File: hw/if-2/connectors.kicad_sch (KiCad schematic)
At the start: 3 parts, among them J1 DB25_Socket, J2 PJ-102AH, J3 Conn_02x12_Odd_Even

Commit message: Documentation improvements, moved a OVP circuit
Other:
- note added: "See: AMP L77SDB25SA4CH4F"
- title: COS/CTCSS/PTT Controls (Radio 1) -> Connectors
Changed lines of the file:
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@@
 	(paper "USLetter")
 	(title_block
-		(title "COS/CTCSS/PTT Controls (Radio 1)")
-		(date "2025-05-13")
+		(title "Connectors")
+		(date "2025-05-31")
 		(rev "2")
 		(company "Bruce MacKinnon KC1FSZ")
@@
 			)
 		)
+	)
+	(text "See: AMP L77SDB25SA4CH4F"
+		(exclude_from_sim no)
+		(at 101.6 118.618 0)
+		(effects
+			(font
+				(size 1.27 1.27)
+			)
+		)

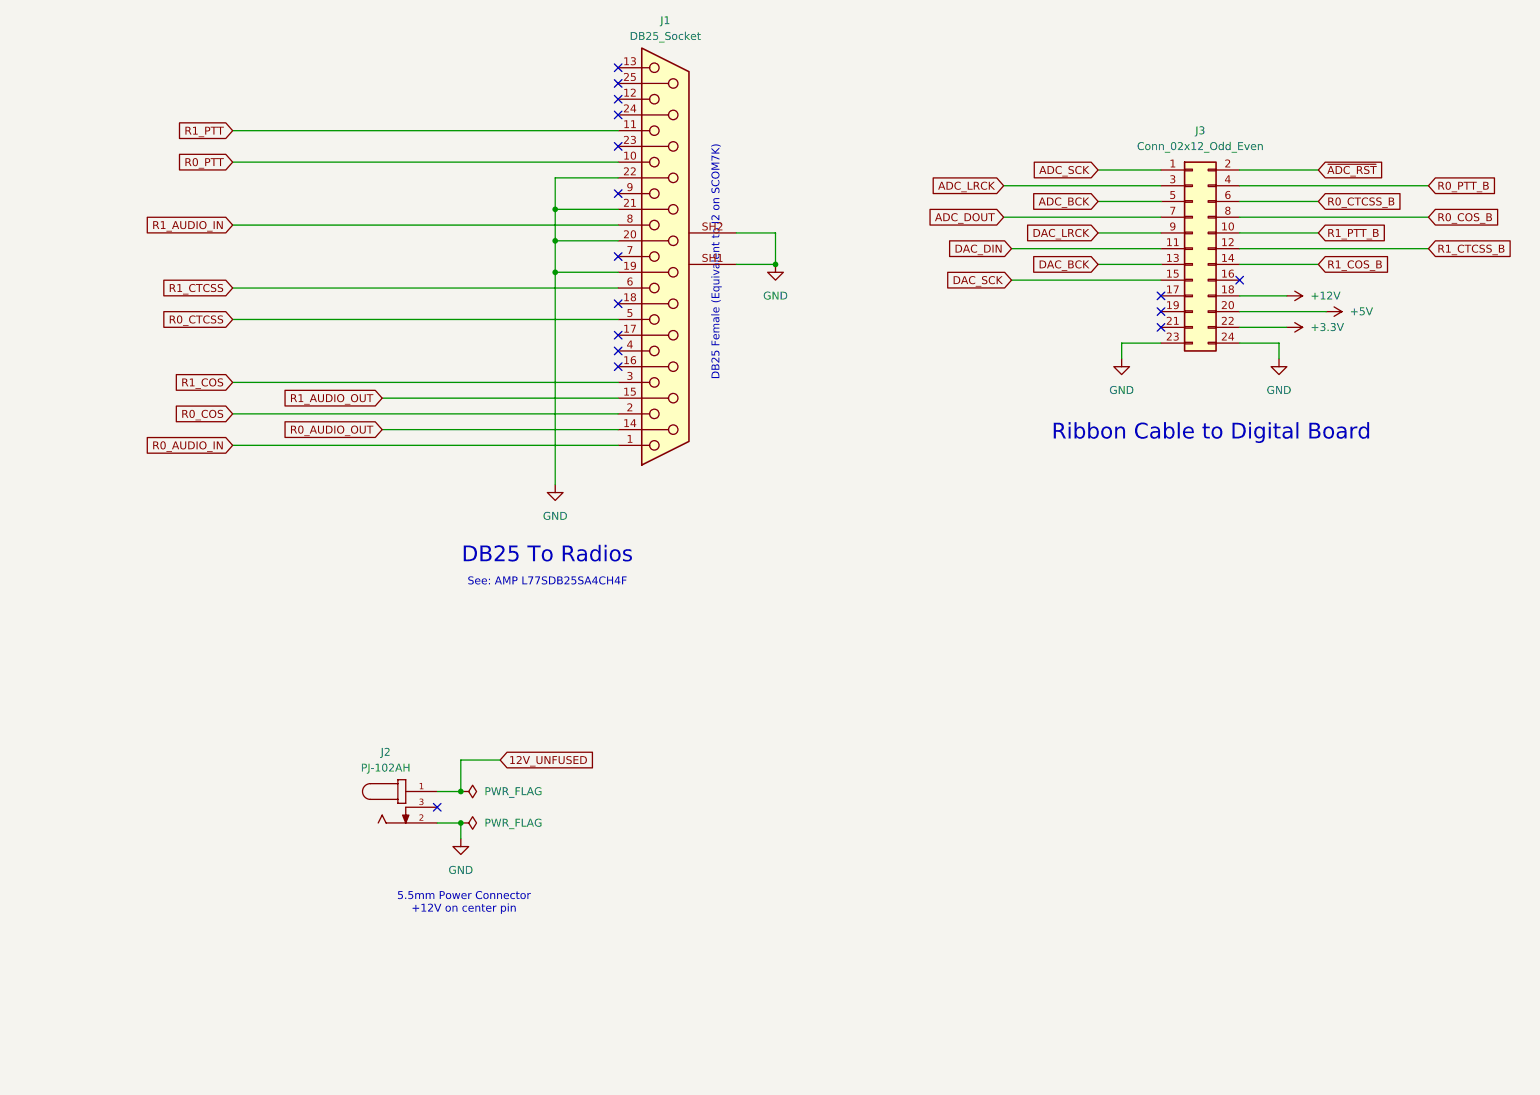
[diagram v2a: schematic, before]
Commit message: Updating schematics, create new mini-board for radio interface
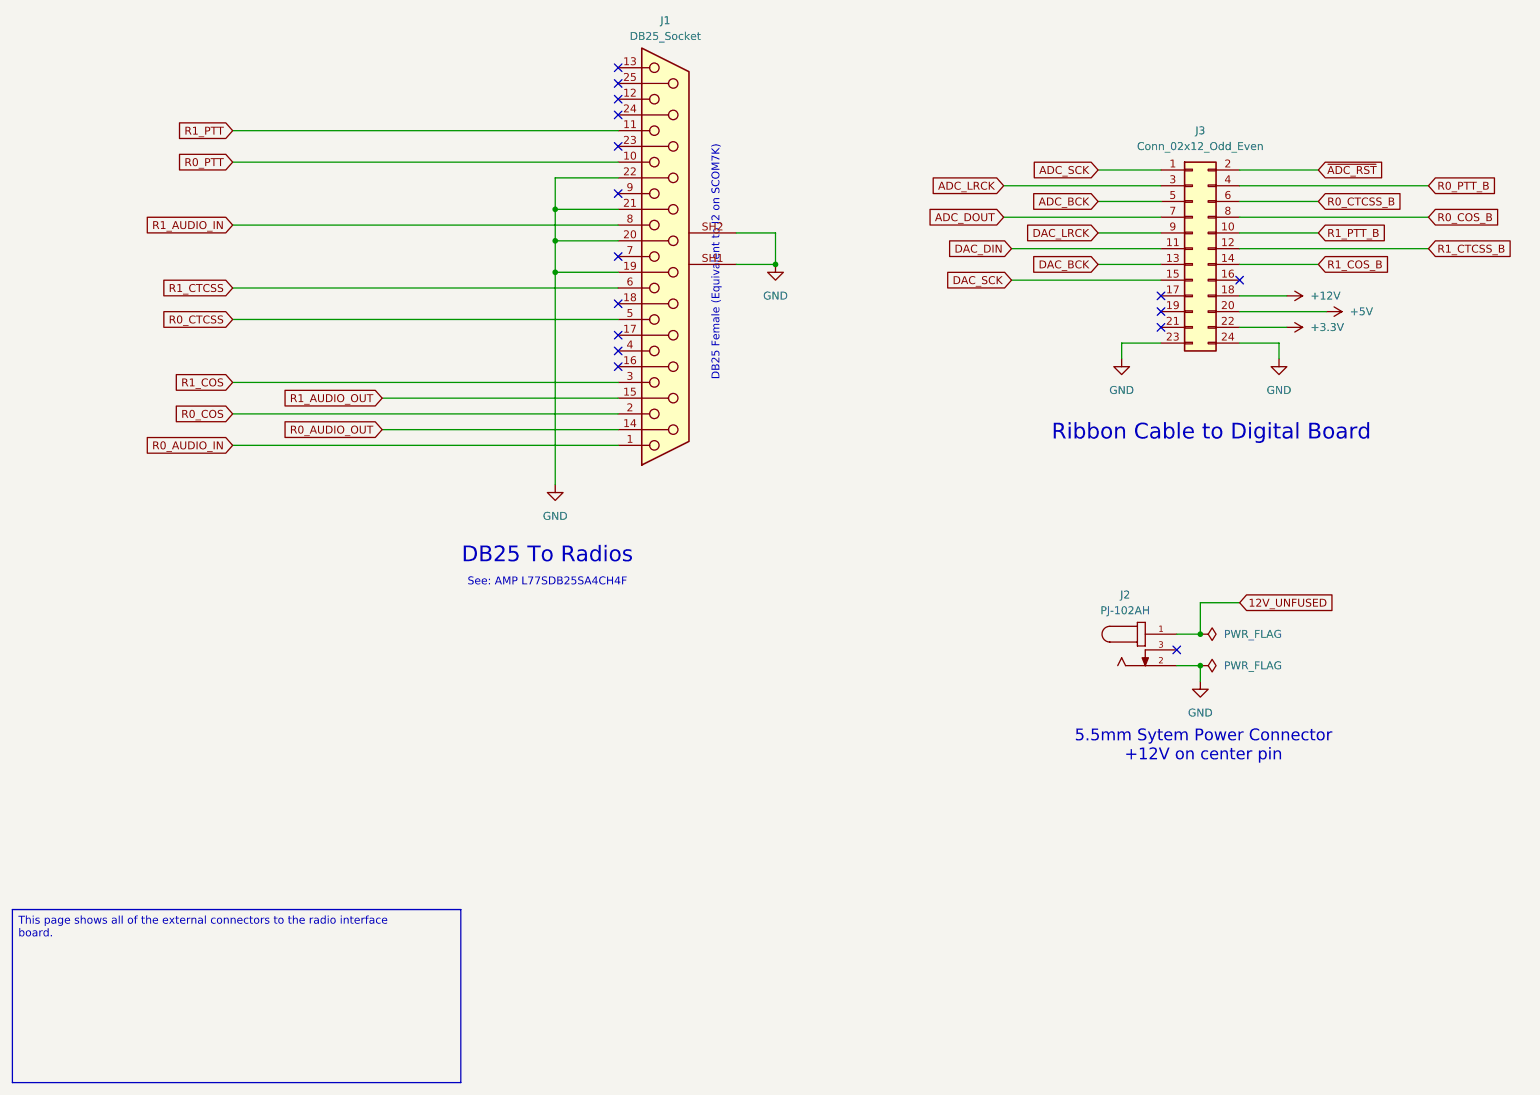
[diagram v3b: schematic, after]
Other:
- note added: "5.5mm Sytem Power Connector +12V on center pin"
- note removed: "5.5mm Power Connector +12V on center pin"
- moved on the sheet: J2
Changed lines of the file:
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@@
 		)
 	)
-	(text "5.5mm Power Connector\n+12V on center pin"
+	(text "5.5mm Sytem Power Connector\n+12V on center pin"
 		(exclude_from_sim no)
-		(at 88.138 170.434 0)
-		(effects
-			(font
-				(size 1.27 1.27)
+		(at 207.518 145.034 0)
+		(effects
+			(font
+				(size 1.905 1.905)
 			)
 		)
@@
 		)
 	)
+	(text_box "This page shows all of the external connectors to the radio interface board.\n"
+		(exclude_from_sim no)
+		(at 15.24 171.45 0)
+		(size 72.39 27.94)
+		(margins 0.9525 0.9525 0.9525 0.9525)
+		(stroke
+			(width 0)
+			(type solid)
+		)
+		(fill
+			(type color)
+			(color 205 245 255 1)
+		)
+		(effects
+			(font
+				(size 1.27 1.27)
+			)
+			(justify left top)
+		)
+	)
 	(junction
-		(at 87.63 152.4)
+		(at 207.01 127)
 		(diameter 0)
 		(color 0 0 0 0)
 	)
 	(junction
-		(at 87.63 157.48)
+		(at 207.01 132.08)
 		(diameter 0)
 		(color 0 0 0 0)
@@
 	)
 	(no_connect
-		(at 83.82 154.94)
+		(at 203.2 129.54)
 	)
 	(no_connect
@@
 	(wire
 		(pts
-			(xy 87.63 147.32) (xy 87.63 152.4)
-		)
-		(stroke
-			(width 0)
-			(type default)
-		)
-	)
-	(wire
-		(pts
-			(xy 87.63 147.32) (xy 93.98 147.32)
+			(xy 207.01 121.92) (xy 207.01 127)
+		)
+		(stroke
+			(width 0)
+			(type default)
+		)
+	)
+	(wire
+		(pts
+			(xy 207.01 121.92) (xy 213.36 121.92)
 		)
 		(stroke
@@
 	(wire
 		(pts
-			(xy 83.82 152.4) (xy 87.63 152.4)
+			(xy 203.2 127) (xy 207.01 127)
 		)
 		(stroke
@@
 	(wire
 		(pts
-			(xy 83.82 157.48) (xy 87.63 157.48)
+			(xy 203.2 132.08) (xy 207.01 132.08)
 		)
 		(stroke
@@
 	(wire
 		(pts
-			(xy 87.63 157.48) (xy 87.63 160.02)
+			(xy 207.01 132.08) (xy 207.01 134.62)
 		)
 		(stroke
@@
 	(global_label "12V_UNFUSED"
 		(shape input)
-		(at 93.98 147.32 0)
+		(at 213.36 121.92 0)
 		(fields_autoplaced yes)
 		(effects
@@
 		)
 		(property "Intersheetrefs" "${INTERSHEET_REFS}"
-			(at 110.149 147.32 0)
+			(at 229.529 121.92 0)
 			(effects
 				(font
@@
 	(symbol
 		(lib_id "symbol-library-1:Power_5.5mm_PJ-102AH")
-		(at 78.74 154.94 0)
+		(at 198.12 129.54 0)
 		(unit 1)
 		(exclude_from_sim no)
@@
 		(fields_autoplaced yes)
 		(property "Reference" "J2"
-			(at 75.5043 146.05 0)
+			(at 194.8843 120.65 0)
 			(effects
 				(font
@@
 		)
 		(property "Value" "PJ-102AH"
-			(at 75.5043 148.59 0)
+			(at 194.8843 123.19 0)
 			(effects
 				(font
@@
 		)
 		(property "Footprint" "bruce-footprints:Power_5.5mm_CUI_PJ-102AH"
-			(at 78.74 154.94 0)
+			(at 198.12 129.54 0)
 			(effects
 				(font
@@
 		)
 		(property "Datasheet" ""
-			(at 78.74 154.94 0)
+			(at 198.12 129.54 0)
 			(effects
 				(font
@@
 		)
 		(property "Description" ""
-			(at 78.74 154.94 0)
+			(at 198.12 129.54 0)
 			(effects
 				(font
@@
 		)
 		(property "MF" "CUI Devices"
-			(at 78.74 154.94 0)
+			(at 198.12 129.54 0)
 			(effects
 				(font
@@
 		)
 		(property "Purchase-URL" "https://pricing.snapeda.com/search/part/PJ-102AH/?ref=eda"
-			(at 78.74 154.94 0)
+			(at 198.12 129.54 0)
 			(effects
 				(font
@@
 		)
 		(property "Package" "None"
-			(at 78.74 154.94 0)
+			(at 198.12 129.54 0)
 			(effects
 				(font
@@
 		)
 		(property "Price" "None"
-			(at 78.74 154.94 0)
+			(at 198.12 129.54 0)
 			(effects
 				(font
@@
 		)
 		(property "CUI_purchase_URL" "https://www.cuidevices.com/product/interconnect/connectors/dc-power-connectors/jacks/pj-102ah?utm_source=snapeda.com&utm_medium=referral&utm_campaign=snapedaBOM"
-			(at 78.74 154.94 0)
+			(at 198.12 129.54 0)
 			(effects
 				(font
@@
 		)
 		(property "MP" "PJ-102AH"
-			(at 78.74 154.94 0)
+			(at 198.12 129.54 0)
 			(effects
 				(font
@@
 		)
 		(property "Availability" "In Stock"
-			(at 78.74 154.94 0)
+			(at 198.12 129.54 0)
 			(effects
 				(font
@@
 		)
 		(property "Description_1" "2.0 x 6.5 mm, 5.0 A, Horizontal, Through Hole, Tapered Pins, Dc Power Jack Connector"
-			(at 78.74 154.94 0)
+			(at 198.12 129.54 0)
 			(effects
 				(font
@@
 	(symbol
 		(lib_id "power:PWR_FLAG")
-		(at 87.63 152.4 270)
+		(at 207.01 127 270)
 		(unit 1)
 		(exclude_from_sim no)
@@
 		(fields_autoplaced yes)
 		(property "Reference" "#FLG01"
-			(at 89.535 152.4 0)
+			(at 208.915 127 0)
 			(effects
 				(font
@@
 		)
 		(property "Value" "PWR_FLAG"
-			(at 91.44 152.3999 90)
+			(at 210.82 126.9999 90)
 			(effects
 				(font
@@
 		)
 		(property "Footprint" ""
-			(at 87.63 152.4 0)
+			(at 207.01 127 0)
 			(effects
 				(font
@@
 		)
 		(property "Datasheet" "~"
-			(at 87.63 152.4 0)
+			(at 207.01 127 0)
 			(effects
 				(font
@@
 		)
 		(property "Description" "Special symbol for telling ERC where power comes from"
-			(at 87.63 152.4 0)
+			(at 207.01 127 0)
 			(effects
 				(font
@@
 	(symbol
 		(lib_id "power:GND")
-		(at 87.63 160.02 0)
+		(at 207.01 134.62 0)
 		(unit 1)
 		(exclude_from_sim no)
@@
 		(fields_autoplaced yes)
 		(property "Reference" "#PWR03"
-			(at 87.63 166.37 0)
+			(at 207.01 140.97 0)
 			(effects
 				(font
@@
 		)
 		(property "Value" "GND"
-			(at 87.63 165.1 0)
+			(at 207.01 139.7 0)
 			(effects
 				(font
@@
 		)
 		(property "Footprint" ""
-			(at 87.63 160.02 0)
+			(at 207.01 134.62 0)
 			(effects
 				(font
@@
 		)
 		(property "Datasheet" ""
-			(at 87.63 160.02 0)
+			(at 207.01 134.62 0)
 			(effects
 				(font
@@
 		)
 		(property "Description" "Power symbol creates a global label with name \"GND\" , ground"
-			(at 87.63 160.02 0)
+			(at 207.01 134.62 0)
 			(effects
 				(font
@@
 	(symbol
 		(lib_id "power:PWR_FLAG")
-		(at 87.63 157.48 270)
+		(at 207.01 132.08 270)
 		(unit 1)
 		(exclude_from_sim no)
@@
 		(fields_autoplaced yes)
 		(property "Reference" "#FLG02"
-			(at 89.535 157.48 0)
+			(at 208.915 132.08 0)
 			(effects
 				(font
@@
 		)
 		(property "Value" "PWR_FLAG"
-			(at 91.44 157.4799 90)
+			(at 210.82 132.0799 90)
 			(effects
 				(font
@@
 		)
 		(property "Footprint" ""
-			(at 87.63 157.48 0)
+			(at 207.01 132.08 0)
 			(effects
 				(font
@@
 		)
 		(property "Datasheet" "~"
-			(at 87.63 157.48 0)
+			(at 207.01 132.08 0)
 			(effects
 				(font
@@
 		)
 		(property "Description" "Special symbol for telling ERC where power comes from"
-			(at 87.63 157.48 0)
-			(effects
-				(font
+			(at 207.01 132.08 0)
+			(effects
+				(font
